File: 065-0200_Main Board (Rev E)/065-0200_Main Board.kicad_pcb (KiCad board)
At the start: 2 copper layers, 152.5 x 54.6 mm, 177 parts, among them J1 UJ32-C-H-G-H2-SMT-TR, J2 0022035025, J3 0022035025, J4 custom_3p_2mm, J5 custom_2p_2mm, J6 Tag-Connect_TC2030-IDC-NL_2x0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, Q1 WSON-8-1EP_2x2mm_P0.5mm_EP0.9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, SW1 3-1437565-0, U1 QRE1113GR, U10 MSOP-8_3x3mm_P0.65mm, U11 SOT-23-5, U12 SOIC-8_3.9x4.9mm_P1.27mm, U13 SOT-23-6, U14 VSON-10-1EP_3x3mm_P0.5mm_EP1.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, U15 QFN-32-1EP_5x5mm_P0.5mm_EP3.1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, U16 SOT-363_SC-70-6, U2 QRE1113GR, U3 QRE1113GR, U4 BM833, U5 2SMPP03, U6 SOT-23-5, U7 TSSOP-8_3x3mm_P0.65mm, U8 WSON-8-1EP_2x2mm_P0.5mm_EP0.9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, U9 SOIC-8_3.9x4.9mm_P1.27mm, Y1 Crystal_SMD_3215-2Pin_3.2x1.5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

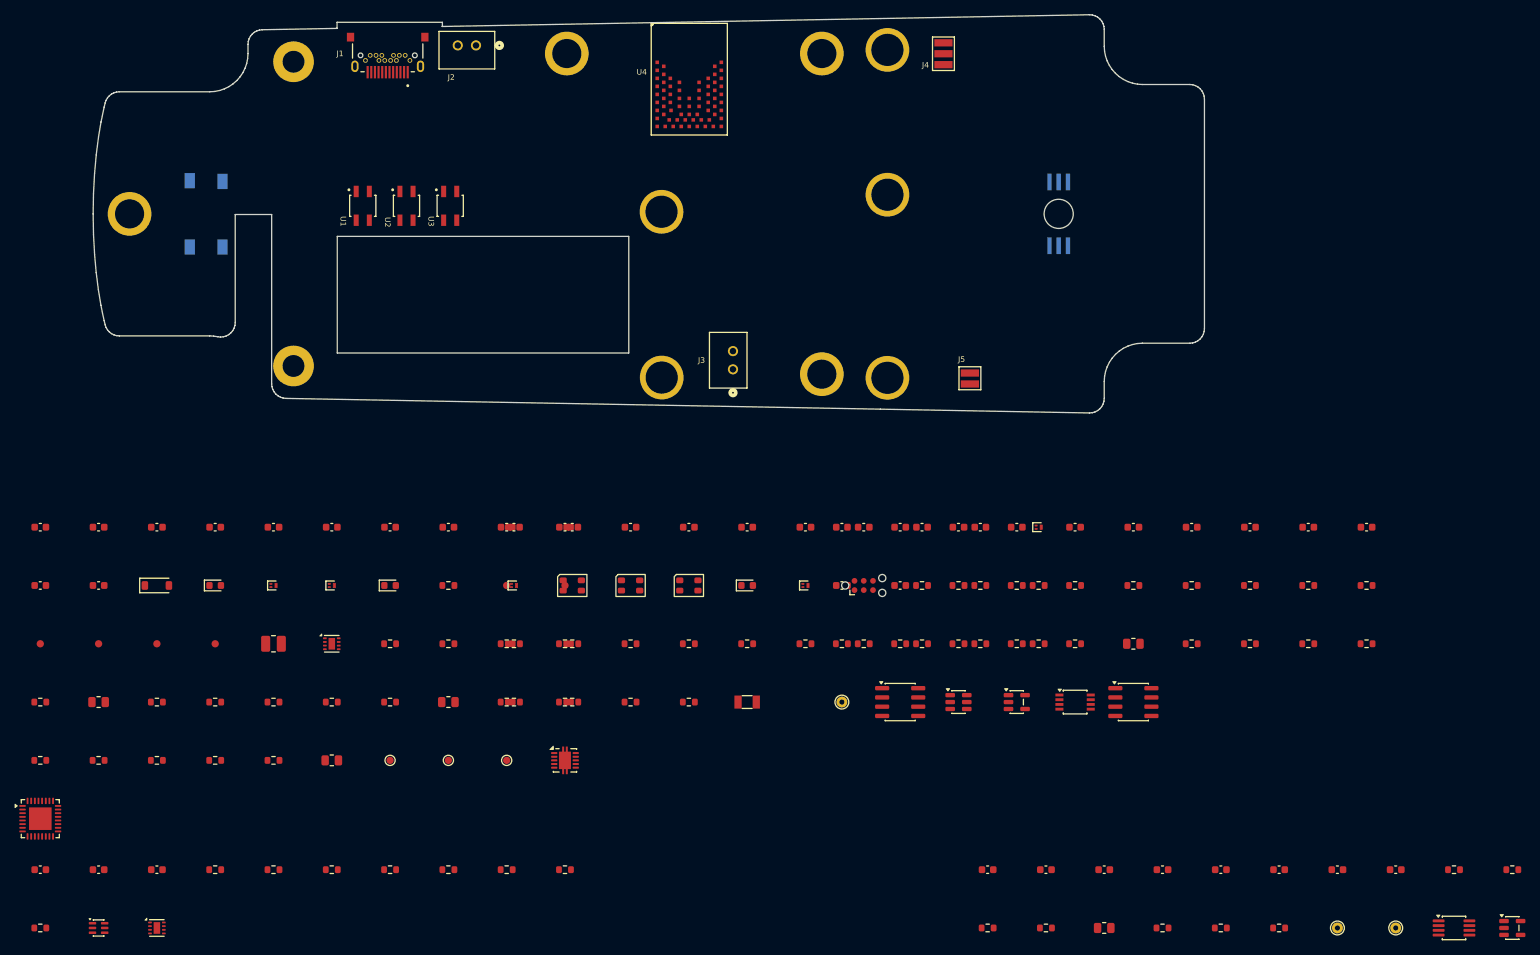
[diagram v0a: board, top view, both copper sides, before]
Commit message: Add OLED display connector to Micro schematic
Added J7 (GME12864-13 OLED) 4-pin I2C connector on Page 3 Micro,
wired to existing SDA/SCL nets shared with the nRF module.

Co-Authored-By: Claude Sonnet 4.6 <noreply@anthropic.com>
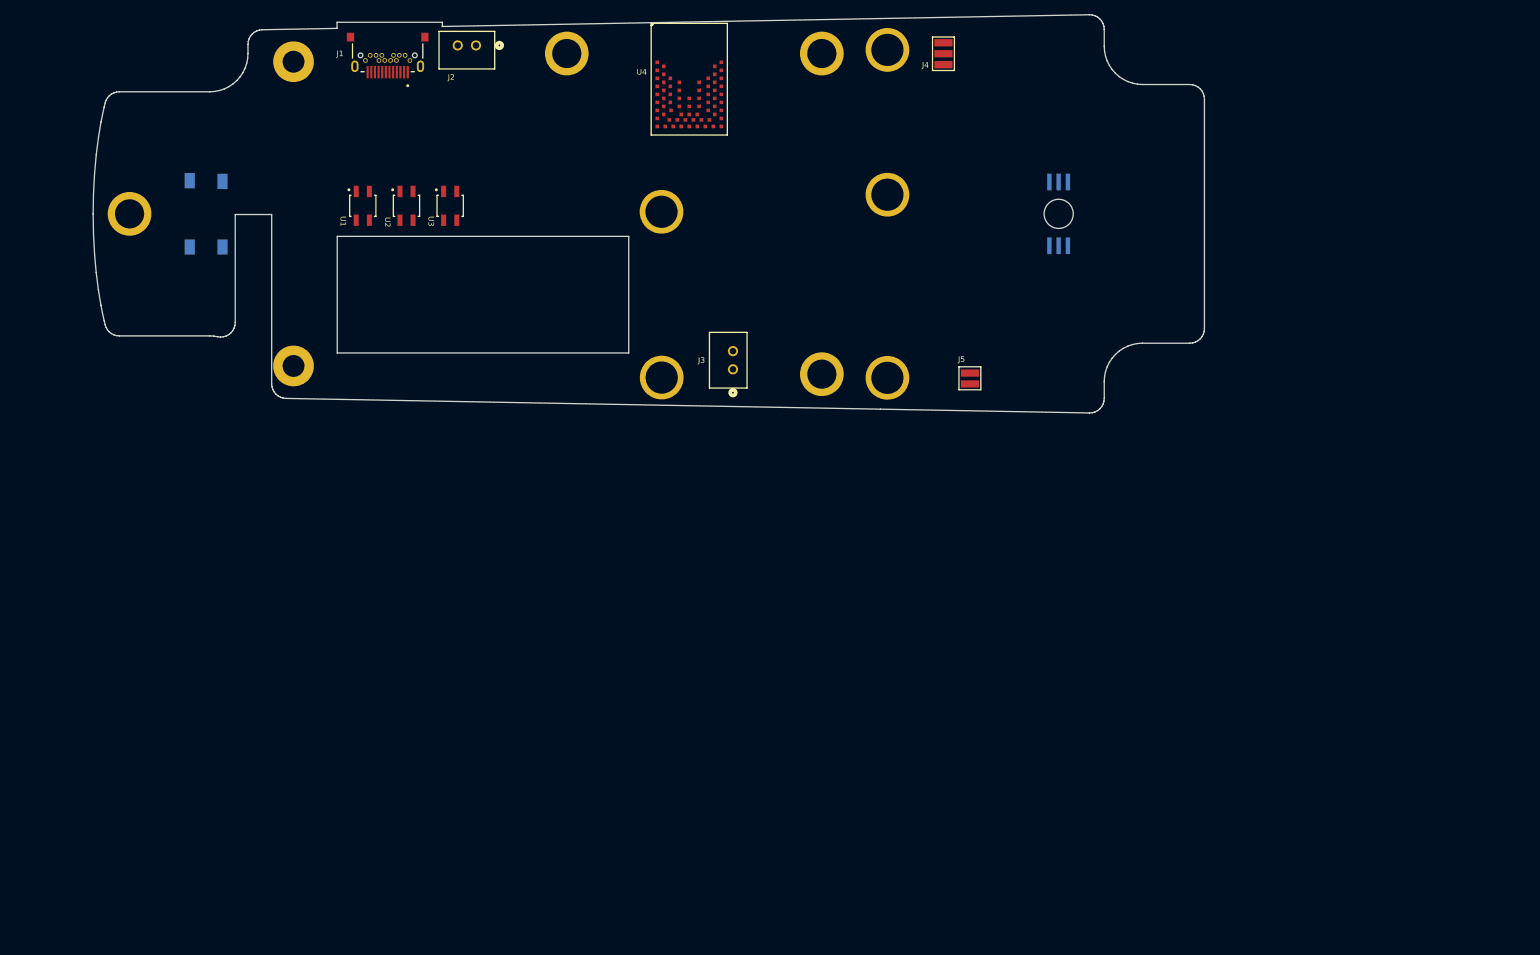
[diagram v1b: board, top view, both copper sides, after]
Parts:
- removed C1, C10, C11, C12, C13, C14, C15, C16, C17, C18, C19, C2, C20, C21, C22, C23, C24, C25, C26, C27, C28, C29, C3, C30, C31, C32, C33, C34, C35, C36, C37, C38, C39, C4, C40, C41, C42, C43, C44, C5, C6, C7, C8, C9: C_0603_1608Metric, Capacitor_SMD:C_0603_1608Metric
- removed D1: D_SOD-123, Diode_SMD:D_SOD-123
- removed D10, D11, D2, D3, D9: SOT-883, Package_TO_SOT_SMD:SOT-883
- removed D12, D7, D8: LED_0603_1608Metric, LED_SMD:LED_0603_1608Metric
- removed D4, D5, D6: LED_Cree-PLCC4_3.2x2.8mm_CCW, LED_SMD:LED_Cree-PLCC4_3.2x2.8mm_CCW
- removed F1, R1, R10, R11, R12, R13, R14, R15, R16, R17, R18, R19, R2, R20, R21, R22, R23, R24, R25, R26, R27, R28, R29, R3, R30, R31, R32, R33, R35, R37, R38, R39, R4, R40, R41, R43, R44, R45, R46, R47, R48, R49, R5, R51, R52, R53, R54, R55, R56, R57, R58, R59, R6, R60, R61, R62, R63, R64, R65, R66, R67, R68, R69, R7, R70, R71, R9: R_0603_1608Metric, Resistor_SMD:R_0603_1608Metric
- removed FD1, FD2, FD3, FD4, FD5, FD6: Fiducial_1mm_Mask2mm, Fiducial:Fiducial_1mm_Mask2mm
- removed J6: Tag-Connect_TC2030-IDC-NL_2x03_P1.27mm_Vertical, Connector:Tag-Connect_TC2030-IDC-NL_2x03_P1.27mm_Vertical
- removed L1: L_1008_2520Metric, Inductor_SMD:L_1008_2520Metric
- removed Q1, U8: WSON-8-1EP_2x2mm_P0.5mm_EP0.9x1.6mm, Package_SON:WSON-8-1EP_2x2mm_P0.5mm_EP0.9x1.6mm
- removed R34, R36, R42, R50, R8: R_0805_2012Metric, Resistor_SMD:R_0805_2012Metric
- removed TP1, TP2, TP7: TestPoint_Pad_D1.0mm, TestPoint:TestPoint_Pad_D1.0mm
- removed TP3, TP4, TP5: TestPoint_THTPad_D1.5mm_Drill0.7mm, TestPoint:TestPoint_THTPad_D1.5mm_Drill0.7mm
- removed U10: MSOP-8_3x3mm_P0.65mm, Package_SO:MSOP-8_3x3mm_P0.65mm
- removed U11, U6: SOT-23-5, Package_TO_SOT_SMD:SOT-23-5
- removed U12, U9: SOIC-8_3.9x4.9mm_P1.27mm, Package_SO:SOIC-8_3.9x4.9mm_P1.27mm
- removed U13: SOT-23-6, Package_TO_SOT_SMD:SOT-23-6
- removed U14: VSON-10-1EP_3x3mm_P0.5mm_EP1.65x2.4mm, Package_SON:VSON-10-1EP_3x3mm_P0.5mm_EP1.65x2.4mm
- removed U15: QFN-32-1EP_5x5mm_P0.5mm_EP3.1x3.1mm, Package_DFN_QFN:QFN-32-1EP_5x5mm_P0.5mm_EP3.1x3.1mm
- removed U16: SOT-363_SC-70-6, Package_TO_SOT_SMD:SOT-363_SC-70-6
- removed U7: TSSOP-8_3x3mm_P0.65mm, Package_SO:TSSOP-8_3x3mm_P0.65mm
- removed Y1: Crystal_SMD_3215-2Pin_3.2x1.5mm, Crystal:Crystal_SMD_3215-2Pin_3.2x1.5mm

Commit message: Place all 155 remaining components on B.Cu off-board
Components grouped by circuit function below/around the board outline,
ready for manual placement. All on B.Cu with layers flipped F↔B.

Co-Authored-By: Claude Sonnet 4.6 <noreply@anthropic.com>
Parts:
- added C1: C_0603_1608Metric, Capacitor_SMD:C_0603_1608Metric, B.Cu at (65.0, 148.0)
- added C10: C_0603_1608Metric, Capacitor_SMD:C_0603_1608Metric, B.Cu at (73.0, 148.0)
- added C11: C_0603_1608Metric, Capacitor_SMD:C_0603_1608Metric, B.Cu at (195.0, 195.0)
- added C12: C_0603_1608Metric, Capacitor_SMD:C_0603_1608Metric, B.Cu at (203.0, 195.0)
- added C13: C_0603_1608Metric, Capacitor_SMD:C_0603_1608Metric, B.Cu at (211.0, 195.0)
- added C14: C_0603_1608Metric, Capacitor_SMD:C_0603_1608Metric, B.Cu at (175.0, 148.0)
- added C15: C_0603_1608Metric, Capacitor_SMD:C_0603_1608Metric, B.Cu at (183.0, 148.0)
- added C16: C_0603_1608Metric, Capacitor_SMD:C_0603_1608Metric, B.Cu at (219.0, 195.0)
- added C17: C_0603_1608Metric, Capacitor_SMD:C_0603_1608Metric, B.Cu at (191.0, 148.0)
- added C18: C_0603_1608Metric, Capacitor_SMD:C_0603_1608Metric, B.Cu at (199.0, 148.0)
- added C19: C_0603_1608Metric, Capacitor_SMD:C_0603_1608Metric, B.Cu at (207.0, 148.0)
- added C2: C_0603_1608Metric, Capacitor_SMD:C_0603_1608Metric, B.Cu at (81.0, 148.0)
- added C20: C_0603_1608Metric, Capacitor_SMD:C_0603_1608Metric, B.Cu at (215.0, 148.0)
- added C21: C_0603_1608Metric, Capacitor_SMD:C_0603_1608Metric, B.Cu at (227.0, 195.0)
- added C22: C_0603_1608Metric, Capacitor_SMD:C_0603_1608Metric, B.Cu at (223.0, 148.0)
- added C23: C_0603_1608Metric, Capacitor_SMD:C_0603_1608Metric, B.Cu at (231.0, 148.0)
- added C24: C_0603_1608Metric, Capacitor_SMD:C_0603_1608Metric, B.Cu at (235.0, 195.0)
- added C25: C_0603_1608Metric, Capacitor_SMD:C_0603_1608Metric, B.Cu at (243.0, 195.0)
- added C26: C_0603_1608Metric, Capacitor_SMD:C_0603_1608Metric, B.Cu at (239.0, 148.0)
- added C27: C_0603_1608Metric, Capacitor_SMD:C_0603_1608Metric, B.Cu at (247.0, 148.0)
- added C28: C_0603_1608Metric, Capacitor_SMD:C_0603_1608Metric, B.Cu at (251.0, 195.0)
- added C29: C_0603_1608Metric, Capacitor_SMD:C_0603_1608Metric, B.Cu at (175.0, 156.0)
- added C3: C_0603_1608Metric, Capacitor_SMD:C_0603_1608Metric, B.Cu at (130.0, 148.0)
- added C30: C_0603_1608Metric, Capacitor_SMD:C_0603_1608Metric, B.Cu at (89.0, 148.0)
- added C31: C_0603_1608Metric, Capacitor_SMD:C_0603_1608Metric, B.Cu at (97.0, 148.0)
- added C32: C_0603_1608Metric, Capacitor_SMD:C_0603_1608Metric, B.Cu at (183.0, 156.0)
- added C33: C_0603_1608Metric, Capacitor_SMD:C_0603_1608Metric, B.Cu at (105.0, 148.0)
- added C34: C_0603_1608Metric, Capacitor_SMD:C_0603_1608Metric, B.Cu at (113.0, 148.0)
- added C35: C_0603_1608Metric, Capacitor_SMD:C_0603_1608Metric, B.Cu at (121.0, 148.0)
- added C36: C_0603_1608Metric, Capacitor_SMD:C_0603_1608Metric, B.Cu at (129.0, 148.0)
- added C37: C_0603_1608Metric, Capacitor_SMD:C_0603_1608Metric, B.Cu at (137.0, 148.0)
- added C38: C_0603_1608Metric, Capacitor_SMD:C_0603_1608Metric, B.Cu at (138.0, 148.0)
- added C39: C_0603_1608Metric, Capacitor_SMD:C_0603_1608Metric, B.Cu at (146.0, 148.0)
- added C4: C_0603_1608Metric, Capacitor_SMD:C_0603_1608Metric, B.Cu at (154.0, 148.0)
- added C40: C_0603_1608Metric, Capacitor_SMD:C_0603_1608Metric, B.Cu at (162.0, 148.0)
- added C41: C_0603_1608Metric, Capacitor_SMD:C_0603_1608Metric, B.Cu at (65.0, 195.0)
- added C42: C_0603_1608Metric, Capacitor_SMD:C_0603_1608Metric, B.Cu at (73.0, 195.0)
- added C43: C_0603_1608Metric, Capacitor_SMD:C_0603_1608Metric, B.Cu at (81.0, 195.0)
- added C44: C_0603_1608Metric, Capacitor_SMD:C_0603_1608Metric, B.Cu at (65.0, 156.0)
- added C5: C_0603_1608Metric, Capacitor_SMD:C_0603_1608Metric, B.Cu at (170.0, 148.0)
- added C6: C_0603_1608Metric, Capacitor_SMD:C_0603_1608Metric, B.Cu at (178.0, 148.0)
- added C7: C_0603_1608Metric, Capacitor_SMD:C_0603_1608Metric, B.Cu at (186.0, 148.0)
- added C8: C_0603_1608Metric, Capacitor_SMD:C_0603_1608Metric, B.Cu at (194.0, 148.0)
- added C9: C_0603_1608Metric, Capacitor_SMD:C_0603_1608Metric, B.Cu at (73.0, 156.0)
- added D1: D_SOD-123, Diode_SMD:D_SOD-123, B.Cu at (81.0, 156.0)
- added D10: SOT-883, Package_TO_SOT_SMD:SOT-883, B.Cu at (202.0, 148.0)
- added D11: SOT-883, Package_TO_SOT_SMD:SOT-883, B.Cu at (130.0, 156.0)
- added D12: LED_0603_1608Metric, LED_SMD:LED_0603_1608Metric, B.Cu at (89.0, 156.0)
- added D2: SOT-883, Package_TO_SOT_SMD:SOT-883, B.Cu at (97.0, 156.0)
- added D3: SOT-883, Package_TO_SOT_SMD:SOT-883, B.Cu at (105.0, 156.0)
- added D4: LED_Cree-PLCC4_3.2x2.8mm_CCW, LED_SMD:LED_Cree-PLCC4_3.2x2.8mm_CCW, B.Cu at (138.0, 156.0)
- added D5: LED_Cree-PLCC4_3.2x2.8mm_CCW, LED_SMD:LED_Cree-PLCC4_3.2x2.8mm_CCW, B.Cu at (146.0, 156.0)
- added D6: LED_Cree-PLCC4_3.2x2.8mm_CCW, LED_SMD:LED_Cree-PLCC4_3.2x2.8mm_CCW, B.Cu at (154.0, 156.0)
- added D7: LED_0603_1608Metric, LED_SMD:LED_0603_1608Metric, B.Cu at (113.0, 156.0)
- added D8: LED_0603_1608Metric, LED_SMD:LED_0603_1608Metric, B.Cu at (162.0, 156.0)
- added D9: SOT-883, Package_TO_SOT_SMD:SOT-883, B.Cu at (170.0, 156.0)
- added F1: R_0603_1608Metric, Resistor_SMD:R_0603_1608Metric, B.Cu at (121.0, 156.0)
- added FD1: Fiducial_1mm_Mask2mm, Fiducial:Fiducial_1mm_Mask2mm, B.Cu at (129.0, 156.0)
- added FD2: Fiducial_1mm_Mask2mm, Fiducial:Fiducial_1mm_Mask2mm, B.Cu at (137.0, 156.0)
- added FD3: Fiducial_1mm_Mask2mm, Fiducial:Fiducial_1mm_Mask2mm, B.Cu at (65.0, 164.0)
- added FD4: Fiducial_1mm_Mask2mm, Fiducial:Fiducial_1mm_Mask2mm, B.Cu at (73.0, 164.0)
- added FD5: Fiducial_1mm_Mask2mm, Fiducial:Fiducial_1mm_Mask2mm, B.Cu at (81.0, 164.0)
- added FD6: Fiducial_1mm_Mask2mm, Fiducial:Fiducial_1mm_Mask2mm, B.Cu at (89.0, 164.0)
- added J6: Tag-Connect_TC2030-IDC-NL_2x03_P1.27mm_Vertical, Connector:Tag-Connect_TC2030-IDC-NL_2x03_P1.27mm_Vertical, B.Cu at (178.0, 156.0)
- added L1: L_1008_2520Metric, Inductor_SMD:L_1008_2520Metric, B.Cu at (97.0, 164.0)
- added Q1: WSON-8-1EP_2x2mm_P0.5mm_EP0.9x1.6mm, Package_SON:WSON-8-1EP_2x2mm_P0.5mm_EP0.9x1.6mm, B.Cu at (105.0, 164.0)
- added R1: R_0603_1608Metric, Resistor_SMD:R_0603_1608Metric, B.Cu at (113.0, 164.0)
- added R10: R_0603_1608Metric, Resistor_SMD:R_0603_1608Metric, B.Cu at (186.0, 156.0)
- added R11: R_0603_1608Metric, Resistor_SMD:R_0603_1608Metric, B.Cu at (194.0, 156.0)
- added R12: R_0603_1608Metric, Resistor_SMD:R_0603_1608Metric, B.Cu at (202.0, 156.0)
- added R13: R_0603_1608Metric, Resistor_SMD:R_0603_1608Metric, B.Cu at (130.0, 164.0)
- added R14: R_0603_1608Metric, Resistor_SMD:R_0603_1608Metric, B.Cu at (138.0, 164.0)
- added R15: R_0603_1608Metric, Resistor_SMD:R_0603_1608Metric, B.Cu at (146.0, 164.0)
- added R16: R_0603_1608Metric, Resistor_SMD:R_0603_1608Metric, B.Cu at (154.0, 164.0)
- added R17: R_0603_1608Metric, Resistor_SMD:R_0603_1608Metric, B.Cu at (162.0, 164.0)
- added R18: R_0603_1608Metric, Resistor_SMD:R_0603_1608Metric, B.Cu at (191.0, 156.0)
- added R19: R_0603_1608Metric, Resistor_SMD:R_0603_1608Metric, B.Cu at (199.0, 156.0)
- added R2: R_0603_1608Metric, Resistor_SMD:R_0603_1608Metric, B.Cu at (121.0, 164.0)
- added R20: R_0603_1608Metric, Resistor_SMD:R_0603_1608Metric, B.Cu at (259.0, 195.0)
- added R21: R_0603_1608Metric, Resistor_SMD:R_0603_1608Metric, B.Cu at (267.0, 195.0)
- added R22: R_0603_1608Metric, Resistor_SMD:R_0603_1608Metric, B.Cu at (207.0, 156.0)
- added R23: R_0603_1608Metric, Resistor_SMD:R_0603_1608Metric, B.Cu at (195.0, 203.0)
- added R24: R_0603_1608Metric, Resistor_SMD:R_0603_1608Metric, B.Cu at (203.0, 203.0)
- added R25: R_0603_1608Metric, Resistor_SMD:R_0603_1608Metric, B.Cu at (215.0, 156.0)
- added R26: R_0603_1608Metric, Resistor_SMD:R_0603_1608Metric, B.Cu at (223.0, 156.0)
- added R27: R_0603_1608Metric, Resistor_SMD:R_0603_1608Metric, B.Cu at (231.0, 156.0)
- added R28: R_0603_1608Metric, Resistor_SMD:R_0603_1608Metric, B.Cu at (239.0, 156.0)
- added R29: R_0603_1608Metric, Resistor_SMD:R_0603_1608Metric, B.Cu at (247.0, 156.0)
- added R3: R_0603_1608Metric, Resistor_SMD:R_0603_1608Metric, B.Cu at (129.0, 164.0)
- added R30: R_0603_1608Metric, Resistor_SMD:R_0603_1608Metric, B.Cu at (175.0, 164.0)
- added R31: R_0603_1608Metric, Resistor_SMD:R_0603_1608Metric, B.Cu at (183.0, 164.0)
- added R32: R_0603_1608Metric, Resistor_SMD:R_0603_1608Metric, B.Cu at (191.0, 164.0)
- added R33: R_0603_1608Metric, Resistor_SMD:R_0603_1608Metric, B.Cu at (199.0, 164.0)
- added R34: R_0805_2012Metric, Resistor_SMD:R_0805_2012Metric, B.Cu at (211.0, 203.0)
- added R35: R_0603_1608Metric, Resistor_SMD:R_0603_1608Metric, B.Cu at (207.0, 164.0)
- added R36: R_0805_2012Metric, Resistor_SMD:R_0805_2012Metric, B.Cu at (215.0, 164.0)
- added R37: R_0603_1608Metric, Resistor_SMD:R_0603_1608Metric, B.Cu at (219.0, 203.0)
- added R38: R_0603_1608Metric, Resistor_SMD:R_0603_1608Metric, B.Cu at (223.0, 164.0)
- added R39: R_0603_1608Metric, Resistor_SMD:R_0603_1608Metric, B.Cu at (231.0, 164.0)
- added R4: R_0603_1608Metric, Resistor_SMD:R_0603_1608Metric, B.Cu at (170.0, 164.0)
- added R40: R_0603_1608Metric, Resistor_SMD:R_0603_1608Metric, B.Cu at (137.0, 164.0)
- added R41: R_0603_1608Metric, Resistor_SMD:R_0603_1608Metric, B.Cu at (65.0, 172.0)
- added R42: R_0805_2012Metric, Resistor_SMD:R_0805_2012Metric, B.Cu at (73.0, 172.0)
- added R43: R_0603_1608Metric, Resistor_SMD:R_0603_1608Metric, B.Cu at (239.0, 164.0)
- added R44: R_0603_1608Metric, Resistor_SMD:R_0603_1608Metric, B.Cu at (247.0, 164.0)
- added R45: R_0603_1608Metric, Resistor_SMD:R_0603_1608Metric, B.Cu at (81.0, 172.0)
- added R46: R_0603_1608Metric, Resistor_SMD:R_0603_1608Metric, B.Cu at (89.0, 172.0)
- added R47: R_0603_1608Metric, Resistor_SMD:R_0603_1608Metric, B.Cu at (97.0, 172.0)
- added R48: R_0603_1608Metric, Resistor_SMD:R_0603_1608Metric, B.Cu at (105.0, 172.0)
- added R49: R_0603_1608Metric, Resistor_SMD:R_0603_1608Metric, B.Cu at (113.0, 172.0)
- added R5: R_0603_1608Metric, Resistor_SMD:R_0603_1608Metric, B.Cu at (178.0, 164.0)
- added R50: R_0805_2012Metric, Resistor_SMD:R_0805_2012Metric, B.Cu at (121.0, 172.0)
- added R51: R_0603_1608Metric, Resistor_SMD:R_0603_1608Metric, B.Cu at (129.0, 172.0)
- added R52: R_0603_1608Metric, Resistor_SMD:R_0603_1608Metric, B.Cu at (137.0, 172.0)
- added R53: R_0603_1608Metric, Resistor_SMD:R_0603_1608Metric, B.Cu at (186.0, 164.0)
- added R54: R_0603_1608Metric, Resistor_SMD:R_0603_1608Metric, B.Cu at (65.0, 180.0)
- added R55: R_0603_1608Metric, Resistor_SMD:R_0603_1608Metric, B.Cu at (73.0, 180.0)
- added R56: R_0603_1608Metric, Resistor_SMD:R_0603_1608Metric, B.Cu at (81.0, 180.0)
- added R57: R_0603_1608Metric, Resistor_SMD:R_0603_1608Metric, B.Cu at (194.0, 164.0)
- added R58: R_0603_1608Metric, Resistor_SMD:R_0603_1608Metric, B.Cu at (202.0, 164.0)
- added R59: R_0603_1608Metric, Resistor_SMD:R_0603_1608Metric, B.Cu at (130.0, 172.0)
- added R6: R_0603_1608Metric, Resistor_SMD:R_0603_1608Metric, B.Cu at (138.0, 172.0)
- added R60: R_0603_1608Metric, Resistor_SMD:R_0603_1608Metric, B.Cu at (89.0, 195.0)
- added R61: R_0603_1608Metric, Resistor_SMD:R_0603_1608Metric, B.Cu at (97.0, 195.0)
- added R62: R_0603_1608Metric, Resistor_SMD:R_0603_1608Metric, B.Cu at (105.0, 195.0)
- added R63: R_0603_1608Metric, Resistor_SMD:R_0603_1608Metric, B.Cu at (113.0, 195.0)
- added R64: R_0603_1608Metric, Resistor_SMD:R_0603_1608Metric, B.Cu at (146.0, 172.0)
- added R65: R_0603_1608Metric, Resistor_SMD:R_0603_1608Metric, B.Cu at (121.0, 195.0)
- added R66: R_0603_1608Metric, Resistor_SMD:R_0603_1608Metric, B.Cu at (129.0, 195.0)
- added R67: R_0603_1608Metric, Resistor_SMD:R_0603_1608Metric, B.Cu at (137.0, 195.0)
- added R68: R_0603_1608Metric, Resistor_SMD:R_0603_1608Metric, B.Cu at (65.0, 203.0)
- added R69: R_0603_1608Metric, Resistor_SMD:R_0603_1608Metric, B.Cu at (89.0, 180.0)
- added R7: R_0603_1608Metric, Resistor_SMD:R_0603_1608Metric, B.Cu at (97.0, 180.0)
- added R70: R_0603_1608Metric, Resistor_SMD:R_0603_1608Metric, B.Cu at (227.0, 203.0)
- added R71: R_0603_1608Metric, Resistor_SMD:R_0603_1608Metric, B.Cu at (235.0, 203.0)
- added R8: R_0805_2012Metric, Resistor_SMD:R_0805_2012Metric, B.Cu at (105.0, 180.0)
- added R9: R_0603_1608Metric, Resistor_SMD:R_0603_1608Metric, B.Cu at (154.0, 172.0)
- added TP1: TestPoint_Pad_D1.0mm, TestPoint:TestPoint_Pad_D1.0mm, B.Cu at (113.0, 180.0)
- added TP2: TestPoint_Pad_D1.0mm, TestPoint:TestPoint_Pad_D1.0mm, B.Cu at (121.0, 180.0)
- added TP3: TestPoint_THTPad_D1.5mm_Drill0.7mm, TestPoint:TestPoint_THTPad_D1.5mm_Drill0.7mm, B.Cu at (175.0, 172.0)
- added TP4: TestPoint_THTPad_D1.5mm_Drill0.7mm, TestPoint:TestPoint_THTPad_D1.5mm_Drill0.7mm, B.Cu at (243.0, 203.0)
- added TP5: TestPoint_THTPad_D1.5mm_Drill0.7mm, TestPoint:TestPoint_THTPad_D1.5mm_Drill0.7mm, B.Cu at (251.0, 203.0)
- added TP7: TestPoint_Pad_D1.0mm, TestPoint:TestPoint_Pad_D1.0mm, B.Cu at (129.0, 180.0)
- added U10: MSOP-8_3x3mm_P0.65mm, Package_SO:MSOP-8_3x3mm_P0.65mm, B.Cu at (259.0, 203.0)
- added U11: SOT-23-5, Package_TO_SOT_SMD:SOT-23-5, B.Cu at (267.0, 203.0)
- added U12: SOIC-8_3.9x4.9mm_P1.27mm, Package_SO:SOIC-8_3.9x4.9mm_P1.27mm, B.Cu at (183.0, 172.0)
- added U13: SOT-23-6, Package_TO_SOT_SMD:SOT-23-6, B.Cu at (191.0, 172.0)
- added U14: VSON-10-1EP_3x3mm_P0.5mm_EP1.65x2.4mm, Package_SON:VSON-10-1EP_3x3mm_P0.5mm_EP1.65x2.4mm, B.Cu at (137.0, 180.0)
- added U15: QFN-32-1EP_5x5mm_P0.5mm_EP3.1x3.1mm, Package_DFN_QFN:QFN-32-1EP_5x5mm_P0.5mm_EP3.1x3.1mm, B.Cu at (65.0, 188.0)
- added U16: SOT-363_SC-70-6, Package_TO_SOT_SMD:SOT-363_SC-70-6, B.Cu at (73.0, 203.0)
- added U6: SOT-23-5, Package_TO_SOT_SMD:SOT-23-5, B.Cu at (199.0, 172.0)
- added U7: TSSOP-8_3x3mm_P0.65mm, Package_SO:TSSOP-8_3x3mm_P0.65mm, B.Cu at (207.0, 172.0)
- added U8: WSON-8-1EP_2x2mm_P0.5mm_EP0.9x1.6mm, Package_SON:WSON-8-1EP_2x2mm_P0.5mm_EP0.9x1.6mm, B.Cu at (81.0, 203.0)
- added U9: SOIC-8_3.9x4.9mm_P1.27mm, Package_SO:SOIC-8_3.9x4.9mm_P1.27mm, B.Cu at (215.0, 172.0)
- added Y1: Crystal_SMD_3215-2Pin_3.2x1.5mm, Crystal:Crystal_SMD_3215-2Pin_3.2x1.5mm, B.Cu at (162.0, 172.0)
